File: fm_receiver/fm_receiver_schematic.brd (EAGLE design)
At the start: 44.4 x 88.6 mm, 22 parts

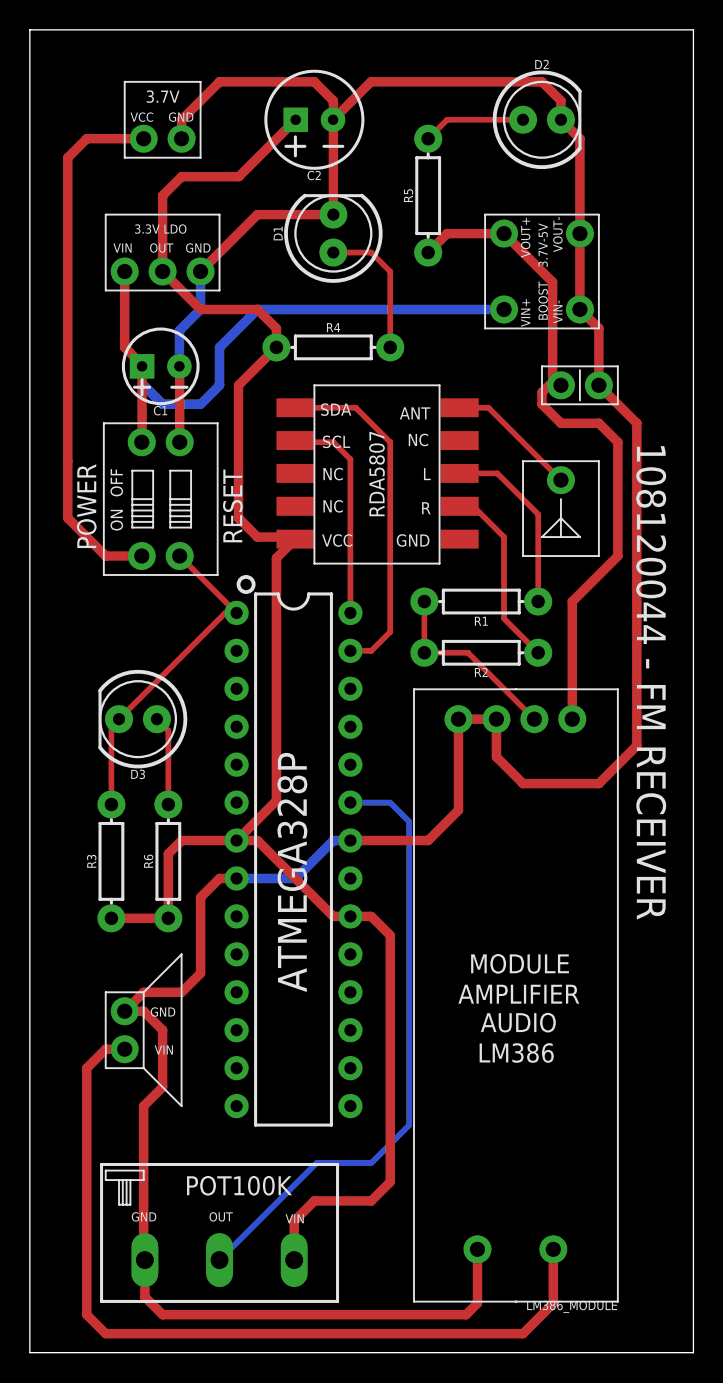
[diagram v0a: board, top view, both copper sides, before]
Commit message: changed round solder pads to long pads, and rerouted traces accordingly to prevent DRC errors
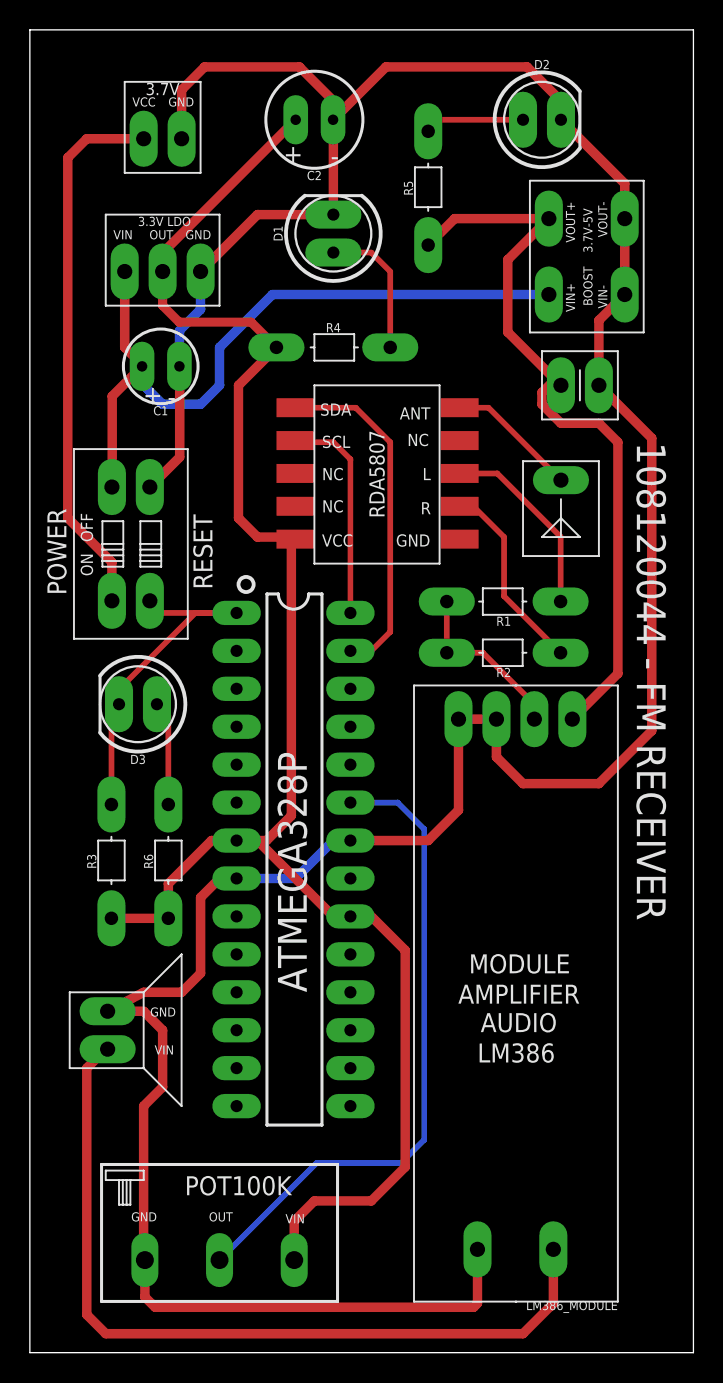
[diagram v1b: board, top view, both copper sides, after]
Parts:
- moved SLIDESWITCH 3.61 mm to (5.49, 50.3)
- moved 3.7_5_BOOST 3.16 mm to (39.8, 75.9)
- moved R1 1.50 mm to (31.7, 50.3)
- moved R2 1.50 mm to (31.7, 46.9)
- moved D3 1.00 mm to (7.24, 43.4)
- moved R5 0.50 mm to (26.7, 78.0)
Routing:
- net GND: track 206.7 -> 217.3 mm
- net 3.7V_UNREG: track 42.0 -> 49.3 mm
- net VCC_5V_BOOST: track 45.4 -> 50.6 mm
- net FRQ_IN: track 41.2 -> 43.5 mm
- net RESET: track 22.1 -> 24.1 mm
- net SPKR_IN: track 55.8 -> 54.7 mm
- net N$12: track 6.03 -> 7.03 mm
- net MONO_IN: track 12.6 -> 11.7 mm
- net VCC_3.3V: track 117.9 -> 117.0 mm
- net N$1: track 35.7 -> 36.5 mm
- net LEFT_OUT: track 12.2 -> 12.9 mm
- net RIGHT_OUT: track 12.5 -> 13.1 mm

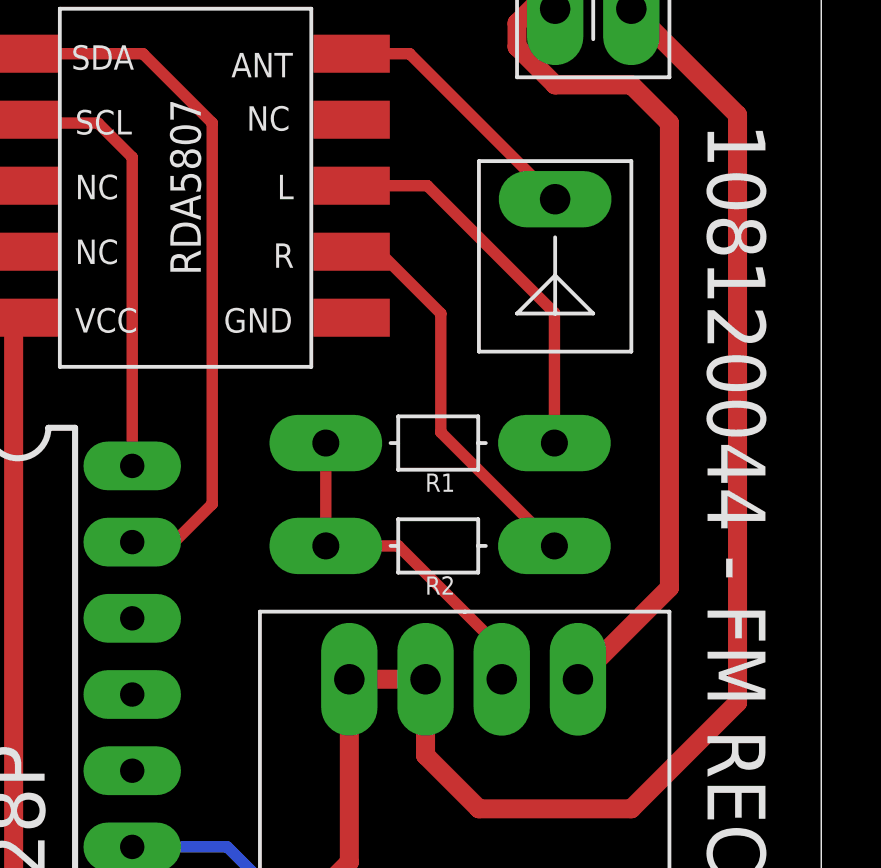
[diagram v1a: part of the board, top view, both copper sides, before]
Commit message: connected crucial GND terminal of RDA5807 to GND net, which was previously missed
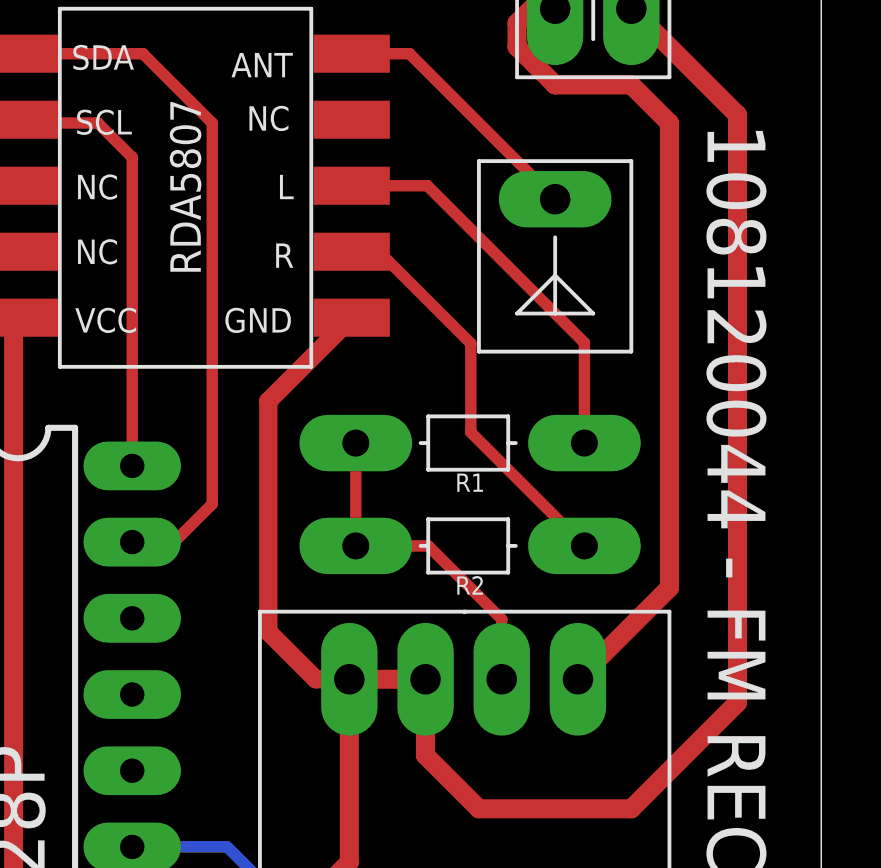
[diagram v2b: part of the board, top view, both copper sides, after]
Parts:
- moved R1 1.00 mm to (32.7, 50.3)
- moved R2 1.00 mm to (32.7, 46.9)
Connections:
- net GND: now also FM_RECEIVER.GND
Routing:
- net GND: track 217.3 -> 232.3 mm
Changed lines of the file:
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@@
 </element>
 <element name="PWR_SUPPLY" library="hridhay_components" library_urn="urn:adsk.eagle:library:38215934" package="3.7V_PWR_DESIGNATOR" package3d_urn="urn:adsk.eagle:package:38237971/2" value="3.7V_PWR_DESIGNATOR" x="7.62" y="81.28" smashed="yes"/>
-<element name="R1" library="SparkFun-Resistors" package="AXIAL-0.3" value="1k" x="31.726" y="50.292" smashed="yes" rot="R180">
-<attribute name="NAME" x="31.726" y="49.276" size="0.6096" layer="25" font="vector" ratio="20" rot="R180" align="bottom-center"/>
-<attribute name="PROD_ID" value="RES-12182" x="-2.564" y="127.762" size="1.778" layer="27" rot="R180" display="off"/>
-<attribute name="VALUE" x="31.726" y="51.308" size="0.6096" layer="27" font="vector" ratio="20" rot="R180" align="top-center"/>
-</element>
-<element name="R2" library="SparkFun-Resistors" package="AXIAL-0.3" value="1k" x="31.726" y="46.863" smashed="yes" rot="R180">
-<attribute name="NAME" x="31.726" y="45.847" size="0.6096" layer="25" font="vector" ratio="20" rot="R180" align="bottom-center"/>
-<attribute name="PROD_ID" value="RES-12182" x="-12.724" y="124.333" size="1.778" layer="27" rot="R180" display="off"/>
-<attribute name="VALUE" x="31.726" y="47.879" size="0.6096" layer="27" font="vector" ratio="20" rot="R180" align="top-center"/>
+<element name="R1" library="SparkFun-Resistors" package="AXIAL-0.3" value="1k" x="32.726" y="50.292" smashed="yes" rot="R180">
+<attribute name="NAME" x="32.726" y="49.276" size="0.6096" layer="25" font="vector" ratio="20" rot="R180" align="bottom-center"/>
+<attribute name="PROD_ID" value="RES-12182" x="-1.564" y="127.762" size="1.778" layer="27" rot="R180" display="off"/>
+<attribute name="VALUE" x="32.726" y="51.308" size="0.6096" layer="27" font="vector" ratio="20" rot="R180" align="top-center"/>
+</element>
+<element name="R2" library="SparkFun-Resistors" package="AXIAL-0.3" value="1k" x="32.726" y="46.863" smashed="yes" rot="R180">
+<attribute name="NAME" x="32.726" y="45.847" size="0.6096" layer="25" font="vector" ratio="20" rot="R180" align="bottom-center"/>
+<attribute name="PROD_ID" value="RES-12182" x="-11.724" y="124.333" size="1.778" layer="27" rot="R180" display="off"/>
+<attribute name="VALUE" x="32.726" y="47.879" size="0.6096" layer="27" font="vector" ratio="20" rot="R180" align="top-center"/>
 </element>
 <element name="R3" library="SparkFun-Resistors" package="AXIAL-0.3" value="10k" x="5.461" y="32.893" smashed="yes" rot="R90">
@@
 <contactref element="FM_RECEIVER" pad="L"/>
 <contactref element="R1" pad="P$1"/>
-<wire x1="35.536" y1="50.292" x2="35.536" y2="54.634" width="0.381" layer="1"/>
+<wire x1="36.536" y1="50.292" x2="36.536" y2="53.634" width="0.381" layer="1"/>
 <wire x1="31.3" y1="58.87" x2="28.78" y2="58.87" width="0.381" layer="1"/>
-<wire x1="35.536" y1="54.634" x2="31.3" y2="58.87" width="0.381" layer="1"/>
+<wire x1="36.536" y1="53.634" x2="31.3" y2="58.87" width="0.381" layer="1"/>
 </signal>
 <signal name="RIGHT_OUT">
 <contactref element="FM_RECEIVER" pad="R"/>
 <contactref element="R2" pad="P$1"/>
-<wire x1="35.536" y1="46.863" x2="31.75" y2="50.649" width="0.381" layer="1"/>
-<wire x1="31.75" y1="50.649" x2="31.75" y2="54.61" width="0.381" layer="1"/>
-<wire x1="31.75" y1="54.61" x2="29.69" y2="56.67" width="0.381" layer="1"/>
+<wire x1="36.536" y1="46.863" x2="32.75" y2="50.649" width="0.381" layer="1"/>
+<wire x1="32.75" y1="50.649" x2="32.75" y2="53.61" width="0.381" layer="1"/>
+<wire x1="32.75" y1="53.61" x2="29.69" y2="56.67" width="0.381" layer="1"/>
 <wire x1="29.69" y1="56.67" x2="28.78" y2="56.67" width="0.381" layer="1"/>
 </signal>
@@
 <wire x1="38.1" y1="64.77" x2="38.1" y2="69.12" width="0.635" layer="1"/>
 <wire x1="38.1" y1="69.12" x2="39.83" y2="70.85" width="0.635" layer="1"/>
+<contactref element="FM_RECEIVER" pad="GND"/>
+<wire x1="28.78" y1="54.47" x2="26" y2="51.69" width="0.6096" layer="1"/>
+<wire x1="26" y1="44" x2="27.582" y2="42.418" width="0.6096" layer="1"/>
+<wire x1="27.582" y1="42.418" x2="28.7" y2="42.418" width="0.6096" layer="1"/>
+<wire x1="26" y1="51.69" x2="26" y2="44" width="0.6096" layer="1"/>
 </signal>
 <signal name="SDA">
@@
 <contactref element="R1" pad="P$2"/>
 <contactref element="LM386_MODULE" pad="VIN"/>
-<wire x1="27.916" y1="50.292" x2="27.916" y2="46.863" width="0.381" layer="1"/>
-<wire x1="27.916" y1="46.863" x2="30.335" y2="46.863" width="0.381" layer="1"/>
-<wire x1="33.78" y1="43.418" x2="33.78" y2="42.418" width="0.381" layer="1"/>
-<wire x1="33.78" y1="43.418" x2="30.335" y2="46.863" width="0.381" layer="1"/>
+<wire x1="28.916" y1="50.292" x2="28.916" y2="46.863" width="0.381" layer="1"/>
+<wire x1="28.916" y1="46.863" x2="31.335" y2="46.863" width="0.381" layer="1"/>
+<wire x1="33.78" y1="44.418" x2="33.78" y2="42.418" width="0.381" layer="1"/>
+<wire x1="33.78" y1="44.418" x2="31.335" y2="46.863" width="0.381" layer="1"/>
 </signal>
 <signal name="N$1">
